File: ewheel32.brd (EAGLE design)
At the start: 160 x 30.5 mm, 202 parts, among them Q1 32.768kHz, Q2 8MHz, U1 MK22DX256VLF5, U10 MC74HC595ADTR2G, U11 MC74HC595ADTR2G, U12 MC74HC595ADTR2G, U13 MC74HC595ADTR2G, U14 MC74HC595ADTR2G, U15 MC74HC595ADTR2G, U16 MC74HC595ADTR2G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

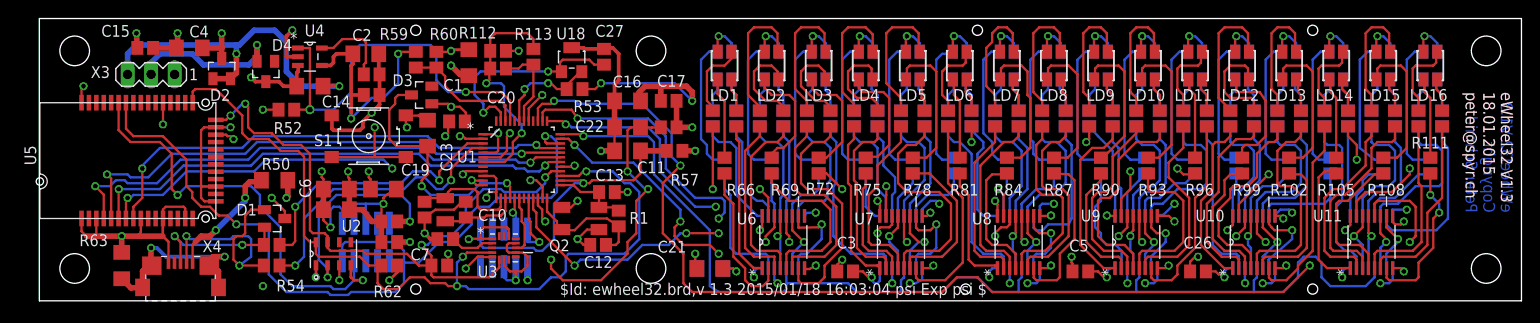
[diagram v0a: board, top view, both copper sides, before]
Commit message: Schottky diode for charger
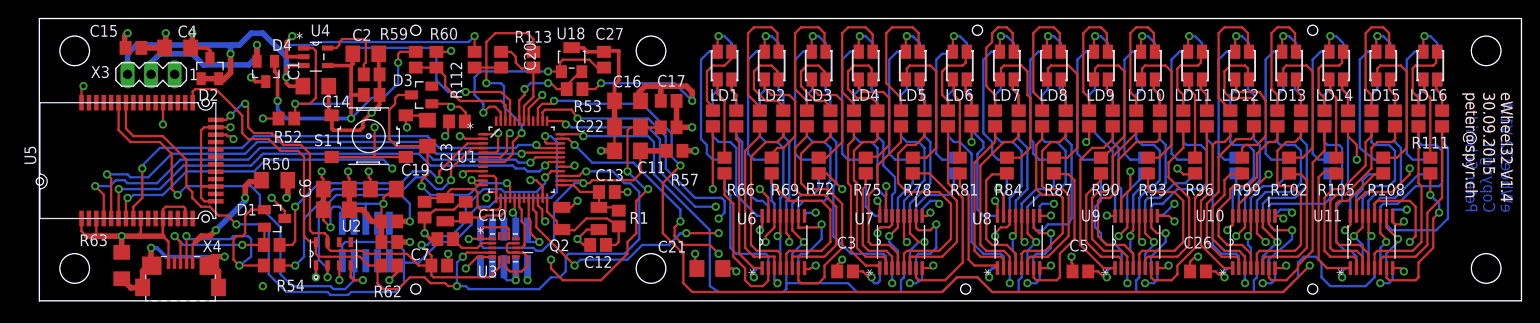
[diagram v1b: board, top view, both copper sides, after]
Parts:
- removed R58: 0, resistor:R1206
- moved C1 16.7 mm to (29.8, 23.2), turned to 0 degrees
- moved R112 2.71 mm to (47.0, 26.0), turned to 90 degrees
- moved C15 1.27 mm to (10.2, 27.3)
- moved C4 1.27 mm to (14.9, 27.3)
- moved D2 1.27 mm to (18.4, 25.1)
- moved C20 1.00 mm to (49.8, 26.0), turned to 90 degrees
- moved R52 0.95 mm to (26.7, 19.7)
- moved U4 0.63 mm to (29.8, 26.4)
- moved C27 0.32 mm to (61.0, 26.0)
- moved R113 0.32 mm to (53.3, 26.0)
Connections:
- removed net N$54: D2.1, D2.2, R58.1, X3.3
- new net VBAT: C1.1, D2.1, D2.2, R112.2, U4.3, X3.3
- net +5V: now also D4.1
- net V+: no longer C1.1, R112.2, R58.2, U4.3
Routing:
- net VBAT: track 0.00 -> 59.1 mm, vias 0 -> 3
- net N$54: track 38.1 -> 0.00 mm, vias 2 -> 0
- net +5V: track 40.9 -> 53.2 mm, vias 3 -> 4
- net V+: track 134.6 -> 125.0 mm, vias 34 -> 32
- net VACCU: track 26.2 -> 28.5 mm
- net CHR-STAT: track 43.1 -> 45.3 mm
- net VA-DIS: track 9.65 -> 10.9 mm
- net GND: track 201.1 -> 202.0 mm
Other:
- board text added: "30.09.2015"
- board text added: "eWheel32 V1.4"
- board text removed: "$Id: ewheel32.brd,v 1.3 2015/01/18 16:03:04 psi Exp psi $"
- board text removed: "18.01.2015"
- board text removed: "eWheel32 V1.3"

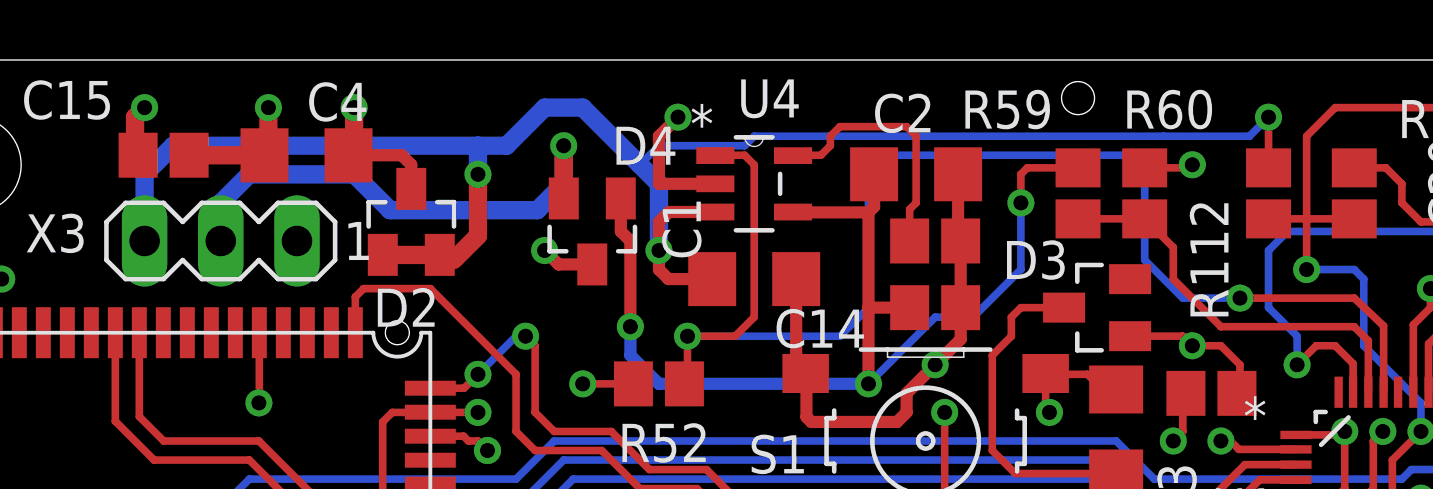
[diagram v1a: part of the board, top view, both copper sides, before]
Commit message: VBAT and V+ are fixed.
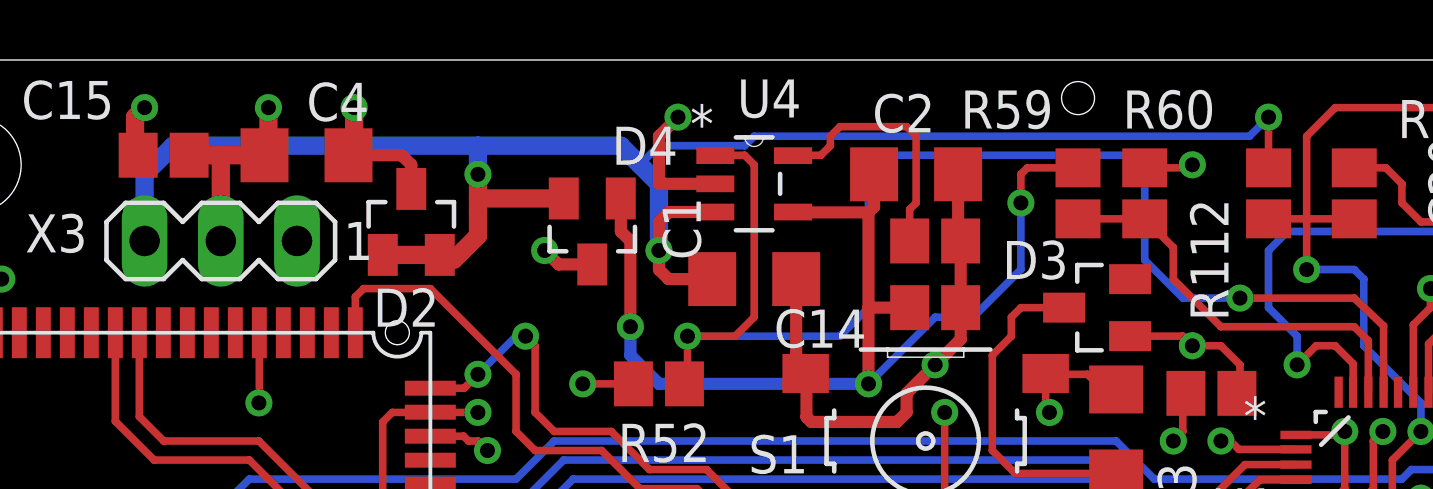
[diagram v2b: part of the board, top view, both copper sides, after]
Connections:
- removed net N$6: D4.2, X3.2
- net V+: now also X3.2
- net VBAT: now also D4.2
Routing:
- net N$6: track 17.0 -> 0.00 mm, vias 1 -> 0
- net V+: track 125.0 -> 127.9 mm
- net VBAT: track 59.1 -> 61.3 mm
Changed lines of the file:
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@@
 <wire x1="50.4825" y1="17.78" x2="50.8" y2="18.0975" width="0.254" layer="1"/>
 <via x="50.8" y="18.0975" extent="1-16" drill="0.5" shape="octagon"/>
-<wire x1="11.01" y1="27.305" x2="13.5225" y2="27.305" width="0.6096" layer="1"/>
+<wire x1="11.01" y1="27.305" x2="12.065" y2="27.305" width="0.6096" layer="1"/>
+<wire x1="12.065" y1="27.305" x2="13.5225" y2="27.305" width="0.6096" layer="1"/>
 <wire x1="50.8" y1="18.0975" x2="50.8" y2="18.7325" width="0.6096" layer="3"/>
 <wire x1="50.8" y1="18.7325" x2="49.53" y2="20.0025" width="0.6096" layer="3"/>
@@
 <wire x1="23.325" y1="23.665" x2="22.86" y2="24.13" width="0.4064" layer="1"/>
 <via x="22.86" y="24.13" extent="1-16" drill="0.5" shape="octagon"/>
+<contactref element="X3" pad="2"/>
+<wire x1="12.065" y1="24.4475" x2="12.065" y2="27.305" width="0.6096" layer="1"/>
 </signal>
 <signal name="UART-TX">
@@
 <contactref element="D2" pad="1"/>
 <via x="20.6375" y="26.67" extent="1-16" drill="0.5" shape="octagon"/>
-<wire x1="20.6375" y1="26.67" x2="20.6375" y2="24.62" width="0.6096" layer="1"/>
+<wire x1="20.6375" y1="26.67" x2="20.6375" y2="25.4" width="0.6096" layer="1"/>
+<wire x1="20.6375" y1="25.4" x2="20.6375" y2="24.62" width="0.6096" layer="1"/>
 <wire x1="9.525" y1="24.4475" x2="9.525" y2="26.67" width="0.6096" layer="16"/>
 <wire x1="9.525" y1="26.67" x2="10.4775" y2="27.6225" width="0.6096" layer="16"/>
@@
 <wire x1="26.67" y1="24.13" x2="26.67" y2="26.3525" width="0.6096" layer="16"/>
 <wire x1="26.67" y1="26.3525" x2="26.035" y2="26.9875" width="0.6096" layer="16"/>
-<wire x1="26.035" y1="26.9875" x2="24.13" y2="28.8925" width="0.6096" layer="16"/>
-<wire x1="24.13" y1="28.8925" x2="22.86" y2="28.8925" width="0.6096" layer="16"/>
-<wire x1="22.86" y1="28.8925" x2="21.59" y2="27.6225" width="0.6096" layer="16"/>
-<wire x1="21.59" y1="27.6225" x2="20.6375" y2="27.6225" width="0.6096" layer="16"/>
+<wire x1="26.035" y1="26.9875" x2="25.4" y2="27.6225" width="0.6096" layer="16"/>
+<wire x1="25.4" y1="27.6225" x2="20.6375" y2="27.6225" width="0.6096" layer="16"/>
 <wire x1="20.6375" y1="24.62" x2="19.83" y2="23.8125" width="0.6096" layer="1"/>
 <wire x1="19.83" y1="23.8125" x2="19.3675" y2="23.8125" width="0.4064" layer="1"/>
@@
 <via x="46.99" y="28.575" extent="1-16" drill="0.5" shape="octagon"/>
 <wire x1="46.99" y1="28.575" x2="46.355" y2="27.94" width="0.254" layer="16"/>
-<wire x1="46.355" y1="27.94" x2="43.4975" y2="27.94" width="0.254" layer="16"/>
-<wire x1="43.4975" y1="27.94" x2="29.845" y2="27.94" width="0.254" layer="16"/>
+<wire x1="46.355" y1="27.94" x2="29.845" y2="27.94" width="0.254" layer="16"/>
 <wire x1="29.845" y1="27.94" x2="29.5275" y2="27.6225" width="0.254" layer="16"/>
 <wire x1="26.035" y1="26.9875" x2="26.67" y2="27.6225" width="0.254" layer="16"/>
 <wire x1="26.67" y1="27.6225" x2="29.5275" y2="27.6225" width="0.254" layer="16"/>
+<contactref element="D4" pad="2"/>
+<wire x1="23.4975" y1="25.865" x2="20.6375" y2="25.865" width="0.6096" layer="1"/>
+<wire x1="20.6375" y1="25.865" x2="20.6375" y2="25.4" width="0.4064" layer="1"/>
 </signal>
 <signal name="BL-LINK">
@@
 <wire x1="38.4175" y1="21.9075" x2="38.4175" y2="21.2725" width="0.254" layer="1"/>
 </signal>
-<signal name="N$6">
-<contactref element="D4" pad="2"/>
-<contactref element="X3" pad="2"/>
-<wire x1="16.51" y1="26.67" x2="17.70560625" y2="25.47439375" width="0.6096" layer="16"/>
-<wire x1="22.61689375" y1="25.47439375" x2="23.495" y2="26.3525" width="0.6096" layer="16"/>
-<wire x1="23.495" y1="26.3525" x2="23.495" y2="27.6225" width="0.6096" layer="16"/>
-<via x="23.495" y="27.6225" extent="1-16" drill="0.5" shape="octagon"/>
-<wire x1="23.495" y1="27.6225" x2="23.495" y2="25.871034375" width="0.6096" layer="1"/>
-<wire x1="23.495" y1="25.871034375" x2="23.4975" y2="25.865" width="0.6096" layer="1" curve="45"/>
-<wire x1="22.61689375" y1="25.47439375" x2="17.70560625" y2="25.47439375" width="0.6096" layer="16"/>
-<wire x1="16.51" y1="26.67" x2="13.0175" y2="26.67" width="0.6096" layer="16"/>
-<wire x1="13.0175" y1="26.67" x2="12.065" y2="25.7175" width="0.6096" layer="16"/>
-<wire x1="12.065" y1="25.7175" x2="12.065" y2="24.4475" width="0.6096" layer="16"/>
-</signal>
 <signal name="SPI-OE">
